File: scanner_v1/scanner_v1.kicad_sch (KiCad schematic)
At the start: 42 parts, among them Q1 SS8050, Q2 SS8050, U2 TS2431BILT, U3 LM321, U4 PIC16F84A-XXSO, U5 LM321, U6 LM321, U7 CH340E, U8 LM7805_TO220, Y1 Crystal

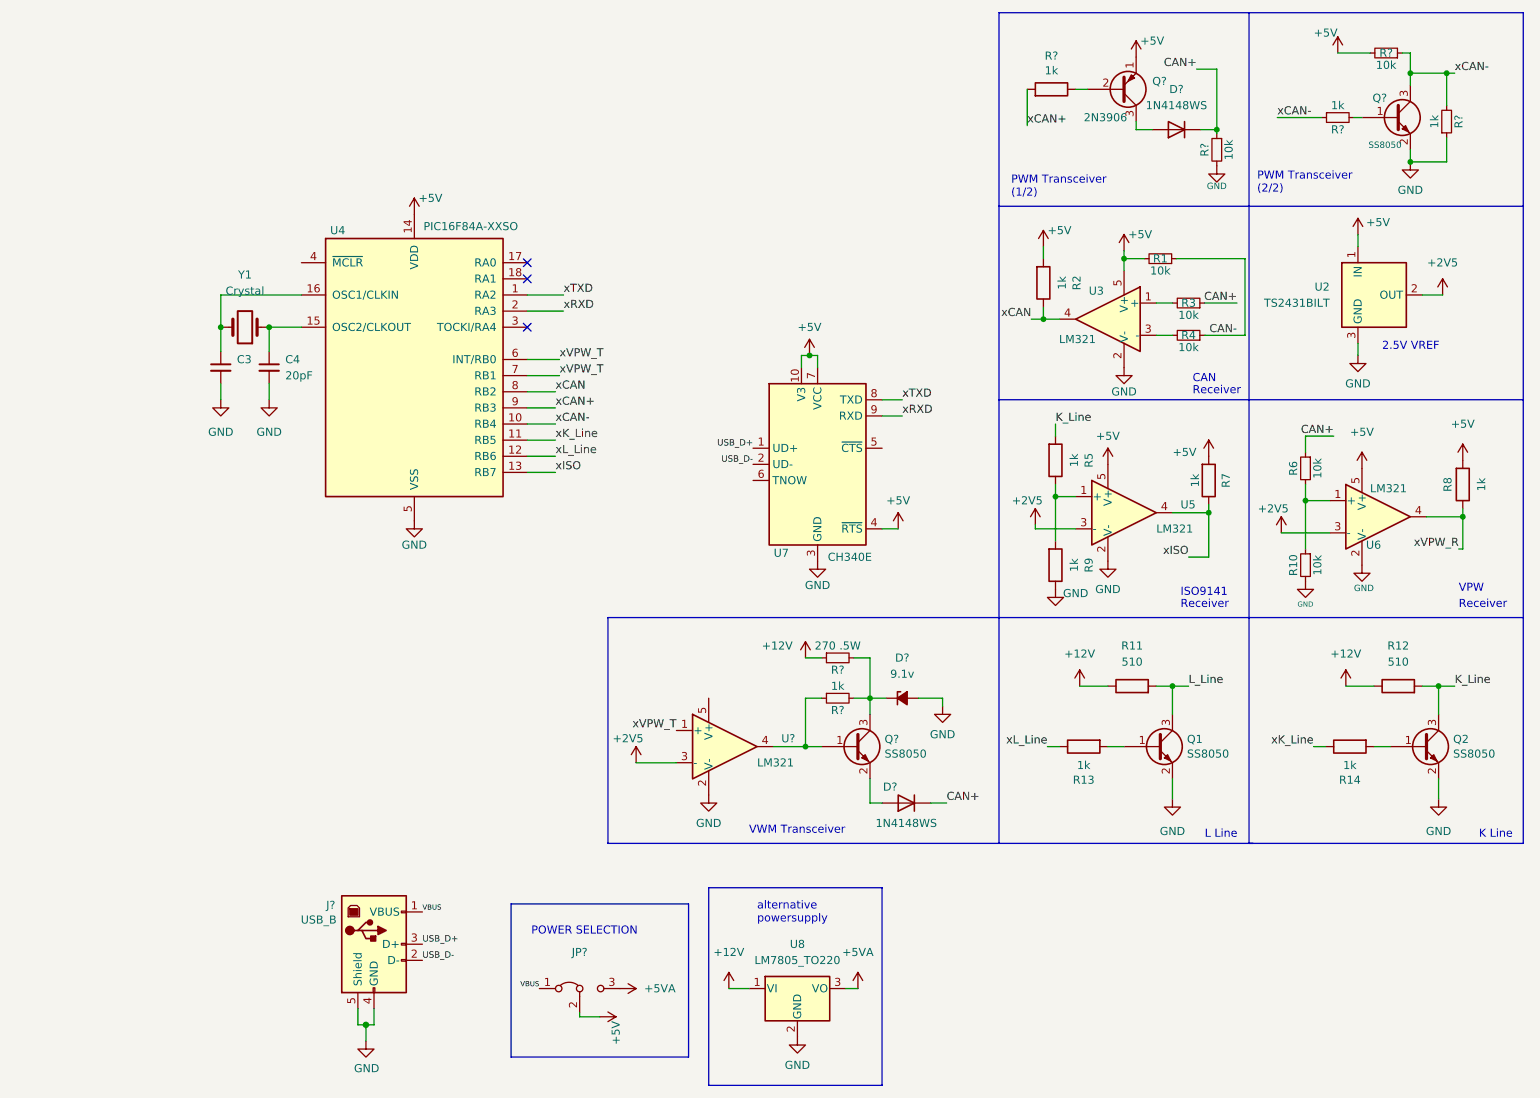
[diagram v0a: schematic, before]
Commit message: added ISO/VPW/PWM receivers
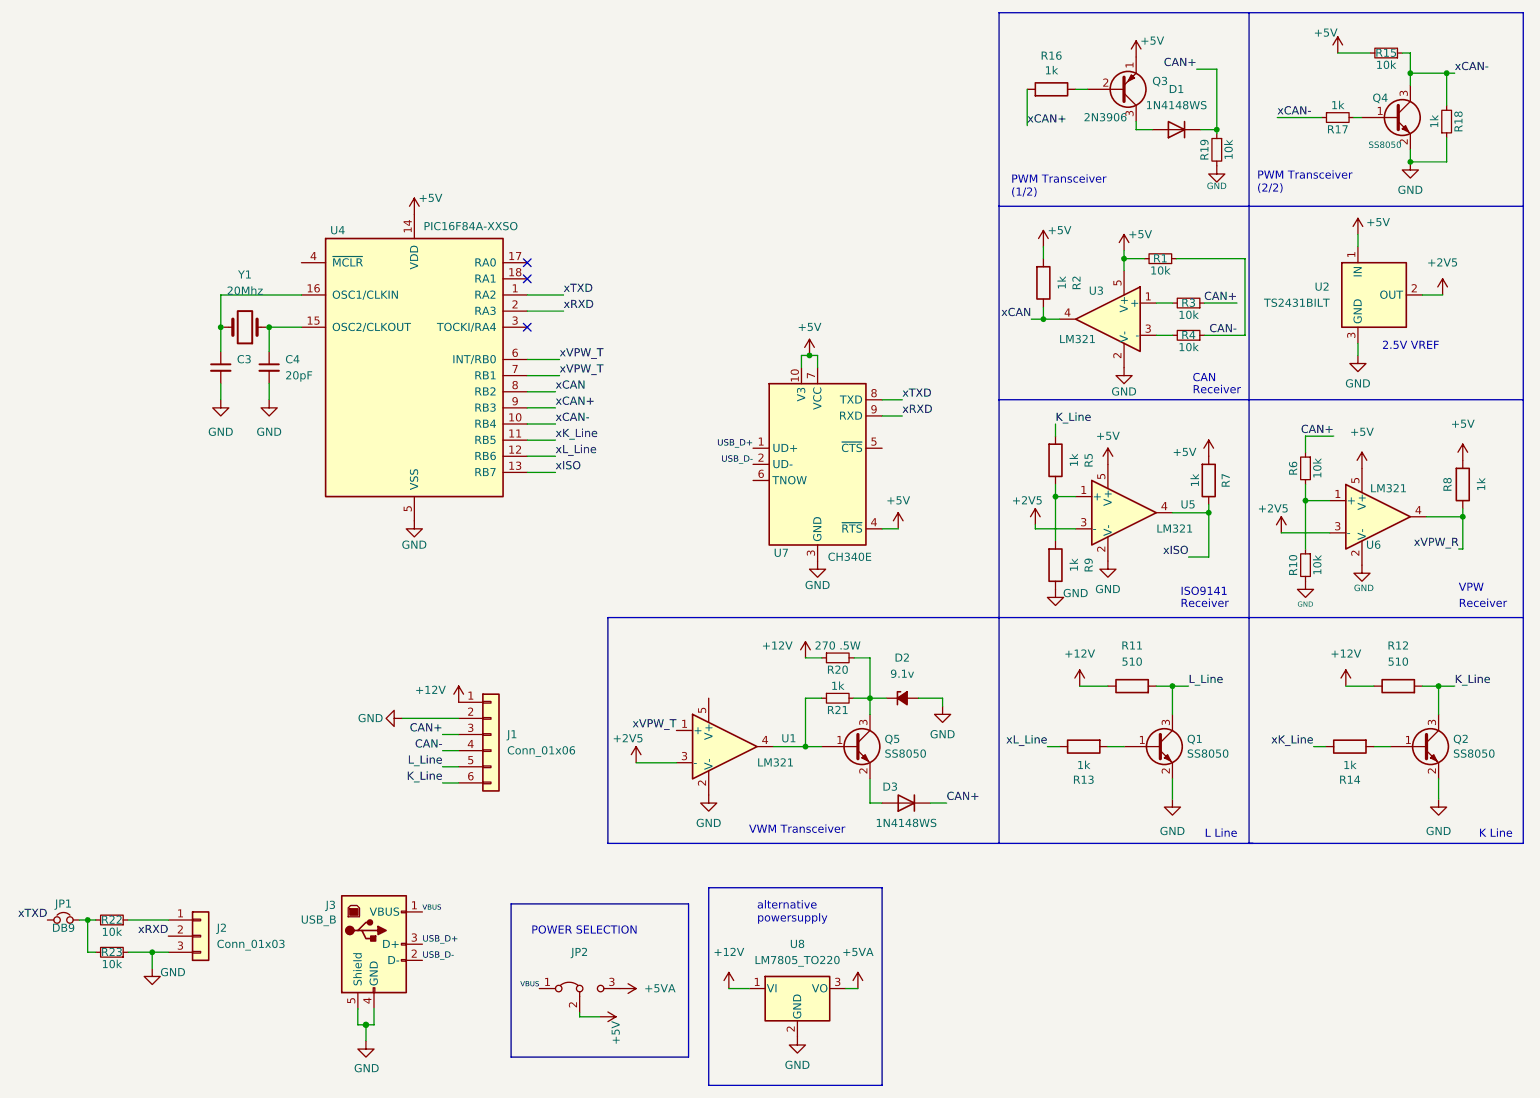
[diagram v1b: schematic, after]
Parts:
- added J1: Conn_01x06, Connector_PinHeader_2.54mm:PinHeader_1x06_P2.54mm_Vertical, symbol Connector_Generic:Conn_01x06
- added J2: Conn_01x03, Connector_PinHeader_2.54mm:PinHeader_1x03_P2.54mm_Vertical, symbol Connector_Generic:Conn_01x03
- added JP1: DB9, Jumper:SolderJumper-2_P1.3mm_Open_TrianglePad1.0x1.5mm, symbol Device:Jumper_NC_Small
- added R22, R23: 10k, Resistor_SMD:R_0603_1608Metric, symbol Device:R_Small
- C3, C4: footprint (none) -> Capacitor_SMD:C_0603_1608Metric
- Q3: renamed from Q?; footprint Package_TO_SOT_SMD:SOT-23_Handsoldering -> Package_TO_SOT_SMD:SOT-23
- Y1: value Crystal -> 20Mhz; footprint (none) -> Crystal:Crystal_HC49-4H_Vertical; LCSC (none) -> C252298
- gave numbers to parts that had none: 15
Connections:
- net +12V: now also J1.1 (Pin_1)
- net CAN+: now also J1.3 (Pin_3)
- net CAN-: now also J1.4 (Pin_4)
- net GND: now also J1.2 (Pin_2), J2.3 (Pin_3), R23.1
- net K_Line: now also J1.6 (Pin_6)
- net L_Line: now also J1.5 (Pin_5)
- net xRXD: now also J2.2 (Pin_2)
- net xTXD: now also JP1.1
- new net: J2.1 (Pin_1), R22.1
- new net: JP1.2, R22.2, R23.2

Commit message: finish v01
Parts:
- added C1, C2: 100nF, Capacitor_SMD:C_0805_2012Metric, symbol Device:C_Small
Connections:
- net +5V: now also U1.5 (V+), C1.1
- net GND: now also C1.2, C2.2
- net VBUS: now also C2.1
- net xVPW_R: now also U4.7 (RB1)
- net xVPW_T: no longer U4.7 (RB1)
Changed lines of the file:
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@@
+    (stroke (width 0) (type default) (color 0 0 0 0))
+  )
+  (wire (pts (xy 146.05 132.08) (xy 146.05 135.255))
     (stroke (width 0) (type default) (color 0 0 0 0))
   )
@@
     (effects (font (size 0.9906 0.9906)) (justify left bottom))
   )
+  (label "VBUS" (at 102.87 181.61 0)
+    (effects (font (size 0.8 0.8)) (justify left bottom))
+  )
   (label "CAN+" (at 104.14 140.97 180)
     (effects (font (size 1.27 1.27)) (justify right bottom))
@@
     (effects (font (size 1.27 1.27)) (justify left bottom))
   )
-  (label "xVPW_T" (at 122.555 84.455 0)
+  (label "xVPW_R" (at 122.555 84.455 0)
     (effects (font (size 1.27 1.27)) (justify left bottom))
   )
@@
     (effects (font (size 1.27 1.27)) (justify right bottom))
   )
+  (symbol (lib_id "power:+5V") (at 80.01 100.33 0) (unit 1)
+    (in_bom yes) (on_board yes)
+    (property "Reference" "#PWR0122" (id 0) (at 80.01 104.14 0)
+      (effects (font (size 1.27 1.27)) hide)
+    )
+    (property "Value" "+5V" (id 1) (at 82.55 97.79 0))
+    (property "Footprint" "" (id 2) (at 80.01 100.33 0)
+      (effects (font (size 1.27 1.27)) hide)
+    )
+    (property "Datasheet" "" (id 3) (at 80.01 100.33 0)
+      (effects (font (size 1.27 1.27)) hide)
+    )
+    (pin "1")
+  )
   (symbol (lib_id "power:+5V") (at 99.695 59.055 0) (unit 1)
     (in_bom yes) (on_board yes)
@@
     (pin "1")
   )
+  (symbol (lib_id "power:+5V") (at 146.05 132.08 0) (unit 1)
+    (in_bom yes) (on_board yes)
+    (property "Reference" "#PWR?" (id 0) (at 146.05 135.89 0)
+      (effects (font (size 1.27 1.27)) hide)
+    )
+    (property "Value" "+5V" (id 1) (at 146.05 127.635 0))
+    (property "Footprint" "" (id 2) (at 146.05 132.08 0)
+      (effects (font (size 1.27 1.27)) hide)
+    )
+    (property "Datasheet" "" (id 3) (at 146.05 132.08 0)
+      (effects (font (size 1.27 1.27)) hide)
+    )
+    (pin "1")
+  )
   (symbol (lib_id "power:+12V") (at 149.225 180.975 0) (unit 1)
     (in_bom yes) (on_board yes) (fields_autoplaced)
@@
     (pin "1")
   )
+  (symbol (lib_id "power:GND") (at 80.01 105.41 0) (unit 1)
+    (in_bom yes) (on_board yes) (fields_autoplaced)
+    (property "Reference" "#PWR0121" (id 0) (at 80.01 111.76 0)
+      (effects (font (size 1.27 1.27)) hide)
+    )
+    (property "Value" "GND" (id 1) (at 80.01 110.49 0))
+    (property "Footprint" "" (id 2) (at 80.01 105.41 0)
+      (effects (font (size 1.27 1.27)) hide)
+    )
+    (property "Datasheet" "" (id 3) (at 80.01 105.41 0)
+      (effects (font (size 1.27 1.27)) hide)
+    )
+    (pin "1")
+  )
   (symbol (lib_id "power:GND") (at 92.075 189.23 0) (unit 1)
     (in_bom yes) (on_board yes)
@@
     )
     (property "Datasheet" "" (id 3) (at 99.695 107.315 0)
+      (effects (font (size 1.27 1.27)) hide)
+    )
+    (pin "1")
+  )
+  (symbol (lib_id "power:GND") (at 102.87 186.69 0) (unit 1)
+    (in_bom yes) (on_board yes)
+    (property "Reference" "#PWR0120" (id 0) (at 102.87 193.04 0)
+      (effects (font (size 1.27 1.27)) hide)
+    )
+    (property "Value" "GND" (id 1) (at 102.9843 191.0144 0))
+    (property "Footprint" "" (id 2) (at 102.87 186.69 0)
+      (effects (font (size 1.27 1.27)) hide)
+    )
+    (property "Datasheet" "" (id 3) (at 102.87 186.69 0)
       (effects (font (size 1.27 1.27)) hide)
     )
@@
     )
     (property "LCSC" "C56475" (id 4) (at 76.835 83.185 0)
+      (effects (font (size 1.27 1.27)) hide)
+    )
+    (pin "1")
+    (pin "2")
+  )
+  (symbol (lib_id "Device:C_Small") (at 80.01 102.87 0) (unit 1)
+    (in_bom yes) (on_board yes)
+    (property "Reference" "C1" (id 0) (at 80.01 101.6 0)
+      (effects (font (size 1.27 1.27)) (justify left))
+    )
+    (property "Value" "100nF" (id 1) (at 81.28 105.41 0)
+      (effects (font (size 1.27 1.27)) (justify left))
+    )
+    (property "Footprint" "Capacitor_SMD:C_0805_2012Metric" (id 2) (at 80.01 102.87 0)
+      (effects (font (size 1.27 1.27)) hide)
+    )
+    (property "Datasheet" "~" (id 3) (at 80.01 102.87 0)
+      (effects (font (size 1.27 1.27)) hide)
+    )
+    (property "LCSC" "C49678" (id 4) (at 80.01 102.87 0)
+      (effects (font (size 1.27 1.27)) hide)
+    )
+    (pin "1")
+    (pin "2")
+  )
+  (symbol (lib_id "Device:C_Small") (at 102.87 184.15 0) (unit 1)
+    (in_bom yes) (on_board yes)
+    (property "Reference" "C2" (id 0) (at 102.87 182.88 0)
+      (effects (font (size 1.27 1.27)) (justify left))
+    )
+    (property "Value" "100nF" (id 1) (at 104.14 186.69 0)
+      (effects (font (size 1.27 1.27)) (justify left))
+    )
+    (property "Footprint" "Capacitor_SMD:C_0805_2012Metric" (id 2) (at 102.87 184.15 0)
+      (effects (font (size 1.27 1.27)) hide)
+    )
+    (property "Datasheet" "~" (id 3) (at 102.87 184.15 0)
+      (effects (font (size 1.27 1.27)) hide)
+    )
+    (property "LCSC" "C49678" (id 4) (at 102.87 184.15 0)
       (effects (font (size 1.27 1.27)) hide)
     )
@@
       (reference "#PWR0119") (unit 1) (value "+5VA") (footprint "")
     )
+    (path "/2af7d829-d25d-4654-9183-b1a361ef0214"
+      (reference "#PWR0120") (unit 1) (value "GND") (footprint "")
+    )
+    (path "/3d9683ba-6a7c-445a-8cca-407358f95350"
+      (reference "#PWR0121") (unit 1) (value "GND") (footprint "")
+    )
+    (path "/5f86faa7-697c-4a4c-8fe1-bdf0d5201dbf"
+      (reference "#PWR0122") (unit 1) (value "+5V") (footprint "")
+    )
+    (path "/383c5886-43f6-4a65-8ad4-8e4d7d39f11d"
+      (reference "#PWR?") (unit 1) (value "+5V") (footprint "")
+    )
+    (path "/333c68c1-f7c8-4029-9353-86bc7338df34"
+      (reference "C1") (unit 1) (value "100nF") (footprint "Capacitor_SMD:C_0805_2012Metric")
+    )
+    (path "/68d85f2e-5682-4f49-af07-a4d381241994"
+      (reference "C2") (unit 1) (value "100nF") (footprint "Capacitor_SMD:C_0805_2012Metric")
+    )
     (path "/227a22d3-70f7-4016-b3b5-3ae6bfff2e1d"

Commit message: v1, fix on RST pin
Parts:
- R1, R10, R15, R19, R22, R23, R3, R4, R6: LCSC (none) -> C25804
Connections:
- net +5V: now also U4.4 (~{MCLR})
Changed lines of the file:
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@@
+    (pin "1")
+  )
+  (symbol (lib_id "power:+5V") (at 81.915 66.675 0) (unit 1)
+    (in_bom yes) (on_board yes)
+    (property "Reference" "#PWR?" (id 0) (at 81.915 70.485 0)
+      (effects (font (size 1.27 1.27)) hide)
+    )
+    (property "Value" "+5V" (id 1) (at 78.74 66.04 0))
+    (property "Footprint" "" (id 2) (at 81.915 66.675 0)
+      (effects (font (size 1.27 1.27)) hide)
+    )
+    (property "Datasheet" "" (id 3) (at 81.915 66.675 0)
+      (effects (font (size 1.27 1.27)) hide)
+    )
     (pin "1")
   )
@@
       (effects (font (size 1.27 1.27)) hide)
     )
+    (property "LCSC" "C25804" (id 4) (at 52.07 170.18 90)
+      (effects (font (size 1.27 1.27)) hide)
+    )
     (pin "1")
     (pin "2")
@@
       (effects (font (size 1.27 1.27)) hide)
     )
+    (property "LCSC" "C25804" (id 4) (at 52.07 175.26 90)
+      (effects (font (size 1.27 1.27)) hide)
+    )
     (pin "1")
     (pin "2")
@@
       (effects (font (size 1.27 1.27)) hide)
     )
+    (property "LCSC" "C25804" (id 4) (at 217.17 66.04 90)
+      (effects (font (size 1.27 1.27)) hide)
+    )
     (pin "1")
     (pin "2")
@@
       (effects (font (size 1.27 1.27)) hide)
     )
+    (property "LCSC" "C25804" (id 4) (at 221.615 73.025 90)
+      (effects (font (size 1.27 1.27)) hide)
+    )
     (pin "1")
     (pin "2")
@@
       (effects (font (size 1.27 1.27)) hide)
     )
+    (property "LCSC" "C25804" (id 4) (at 221.615 78.105 90)
+      (effects (font (size 1.27 1.27)) hide)
+    )
     (pin "1")
     (pin "2")
@@
       (effects (font (size 1.27 1.27)) hide)
     )
+    (property "LCSC" "C25804" (id 4) (at 226.06 48.895 90)
+      (effects (font (size 1.27 1.27)) hide)
+    )
     (pin "1")
     (pin "2")
@@
       (effects (font (size 1.27 1.27)) hide)
     )
+    (property "LCSC" "C25804" (id 4) (at 240.03 99.06 90)
+      (effects (font (size 1.27 1.27)) hide)
+    )
     (pin "1")
     (pin "2")
@@
       (effects (font (size 1.27 1.27)) hide)
     )
+    (property "LCSC" "C25804" (id 4) (at 240.03 114.3 90)
+      (effects (font (size 1.27 1.27)) hide)
+    )
     (pin "1")
     (pin "2")
@@
     )
     (property "Datasheet" "~" (id 3) (at 252.73 33.655 0)
+      (effects (font (size 1.27 1.27)) hide)
+    )
+    (property "LCSC" "C25804" (id 4) (at 252.73 33.655 90)
       (effects (font (size 1.27 1.27)) hide)
     )
@@
       (reference "#PWR?") (unit 1) (value "+5V") (footprint "")
     )
+    (path "/d63de014-a4aa-414e-b672-5d7210671921"
+      (reference "#PWR?") (unit 1) (value "+5V") (footprint "")
+    )
